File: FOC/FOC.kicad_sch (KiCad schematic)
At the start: 8 parts, among them J1 Conn_ARM_JTAG_SWD_10, J2 Conn_01x04, U1 STM32G431CBTx, U2 DRV8311H, U3 SN65HVD230, U4 AP2112K-3.3, Y1 Crystal_GND24

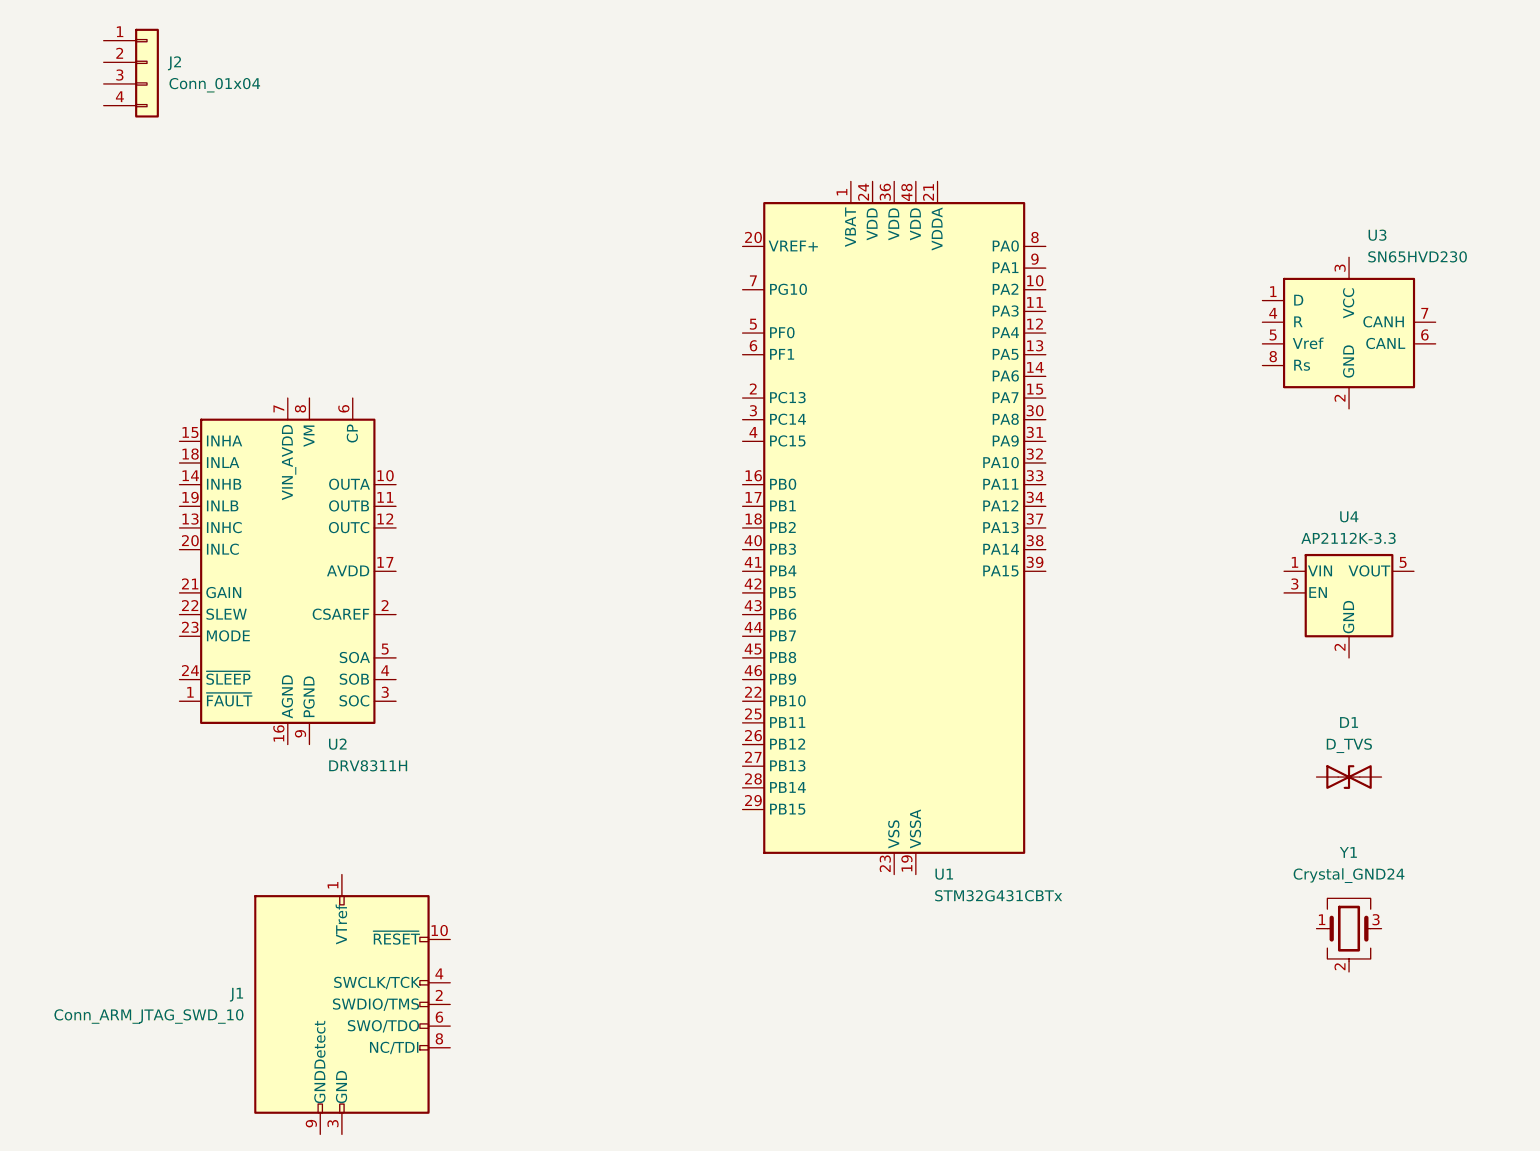
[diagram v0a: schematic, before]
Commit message: mcu module done; CAN transceiver done. todo: controller module + power
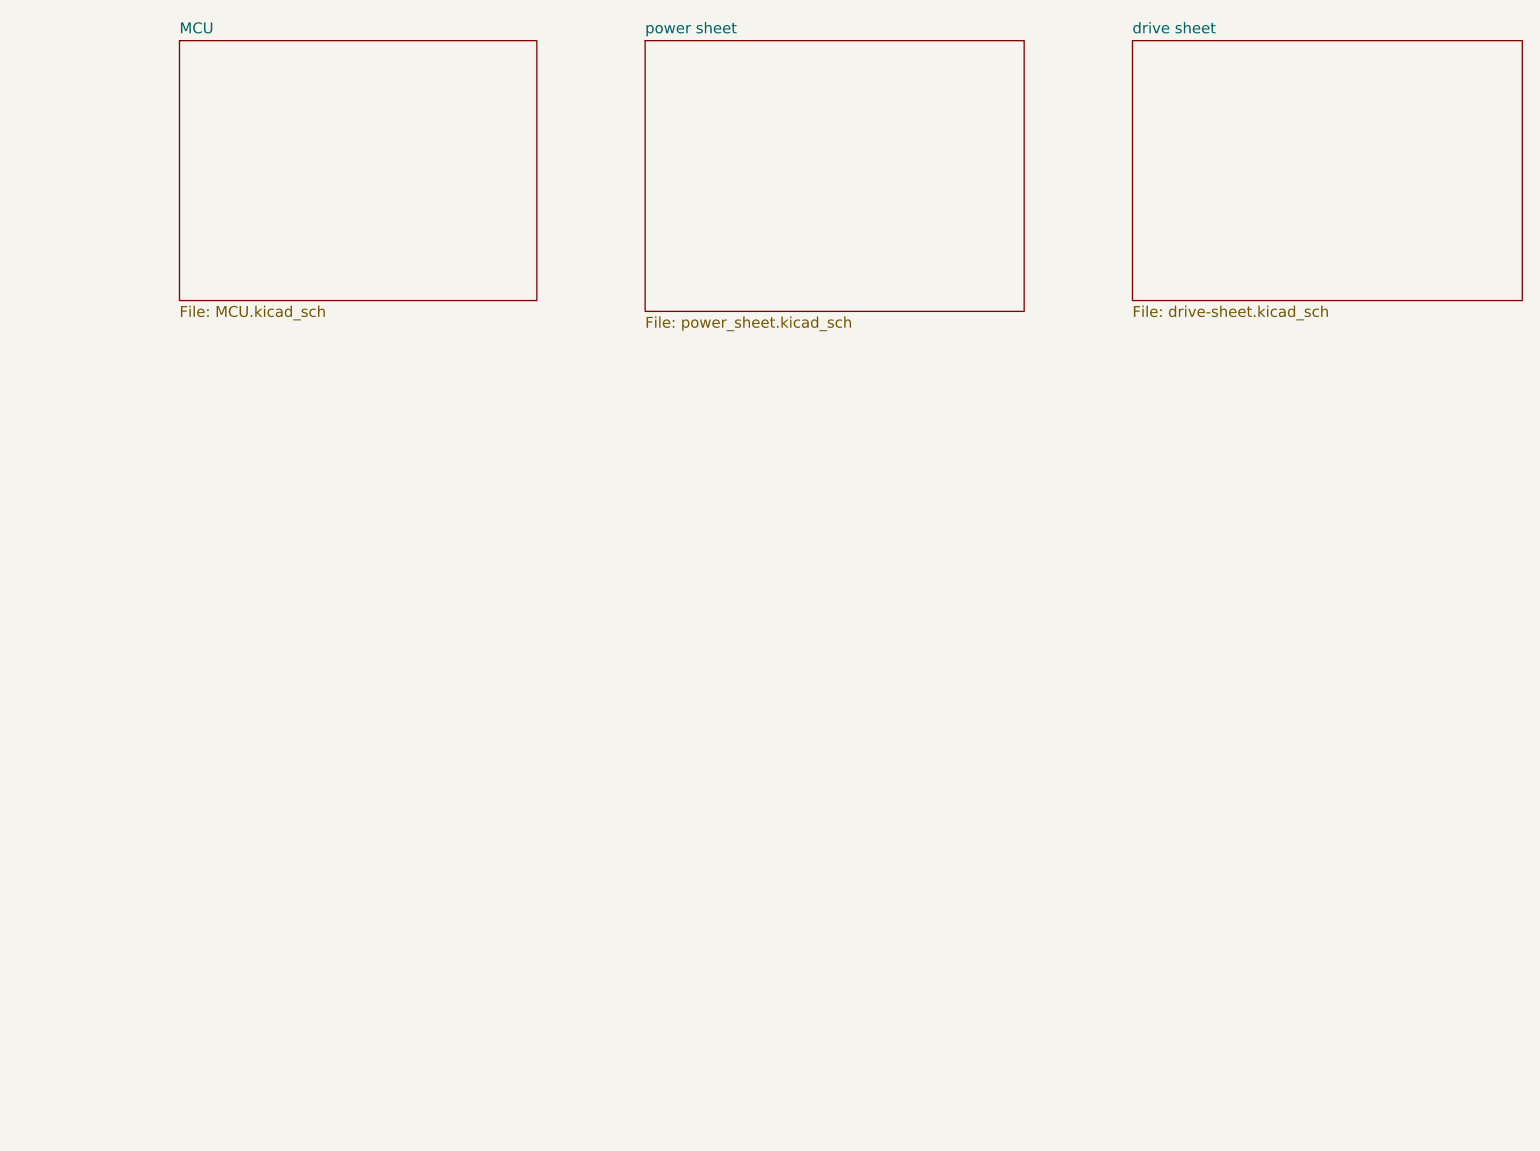
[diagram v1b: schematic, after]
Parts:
- removed D1: D_TVS, symbol Device:D_TVS
- removed J1: Conn_ARM_JTAG_SWD_10, symbol Connector:Conn_ARM_JTAG_SWD_10
- removed J2: Conn_01x04, symbol Connector_Generic:Conn_01x04
- removed U1: STM32G431CBTx, Package_QFP:LQFP-48_7x7mm_P0.5mm, symbol MCU_ST_STM32G4:STM32G431CBTx
- removed U2: DRV8311H, Package_DFN_QFN:Texas_RRW0024A_WQFN-24-1EP_3x3mm_P0.4mm_EP1.9x1.9mm, symbol Driver_Motor:DRV8311H
- removed U3: SN65HVD230, Package_SO:SOIC-8_3.9x4.9mm_P1.27mm, symbol Interface_CAN_LIN:SN65HVD230
- removed U4: AP2112K-3.3, Package_TO_SOT_SMD:SOT-23-5, symbol Regulator_Linear:AP2112K-3.3
- removed Y1: Crystal_GND24, symbol Device:Crystal_GND24
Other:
- added sheet MCU (MCU.kicad_sch)
- added sheet drive sheet (drive-sheet.kicad_sch)
- added sheet power sheet (power_sheet.kicad_sch)

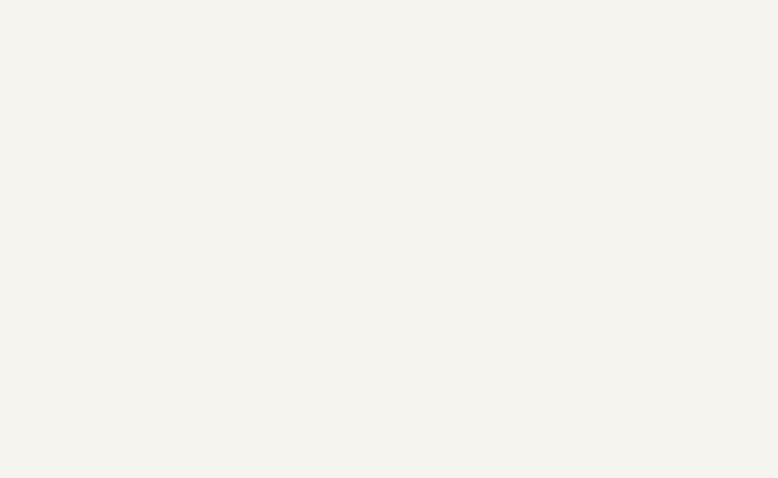
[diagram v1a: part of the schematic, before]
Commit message: mech considered; mounting holes; teardrops
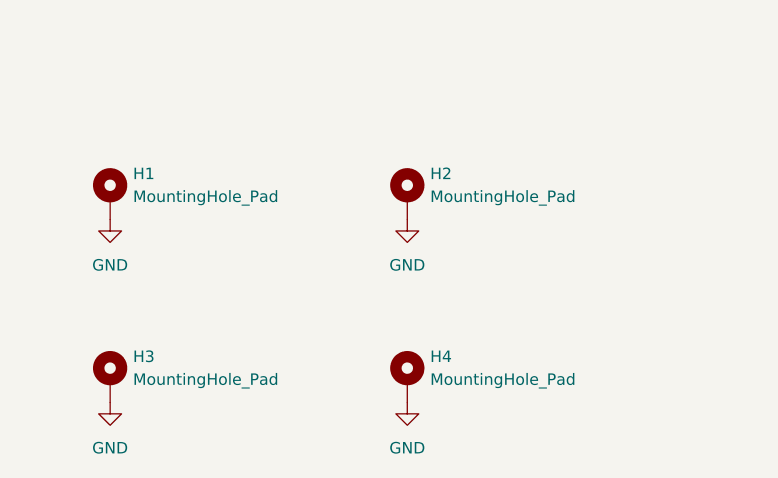
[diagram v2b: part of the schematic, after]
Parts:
- added H1, H2, H3, H4: MountingHole_Pad, MountingHole:MountingHole_2.1mm, symbol Mechanical:MountingHole_Pad
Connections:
- new net GND: H1.1, H2.1, H3.1, H4.1
